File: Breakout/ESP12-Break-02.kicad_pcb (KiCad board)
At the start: 2 copper layers, 22.9 x 66.3 mm, 22 parts, among them J1 CONN_01X08, J2 CONN_01X08, J3 GS2, U1 ESP-12, U2 AP2112K-3.3TRG1

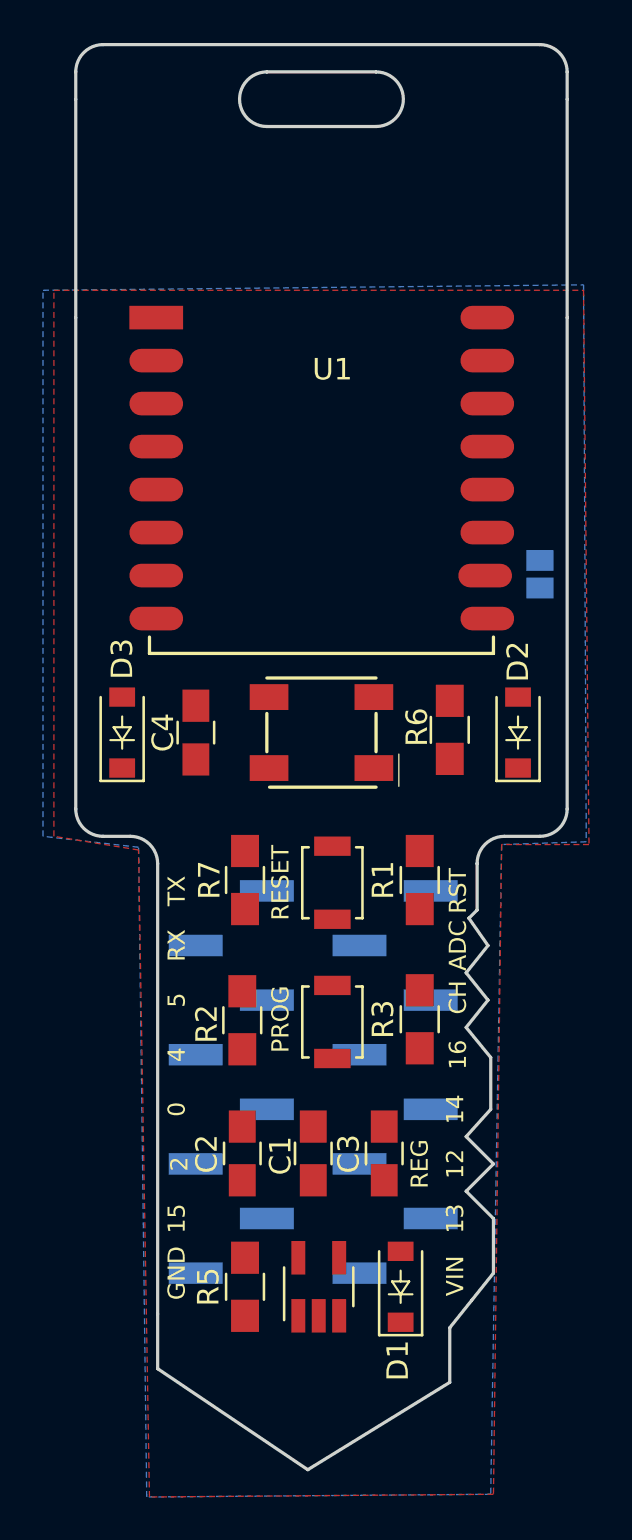
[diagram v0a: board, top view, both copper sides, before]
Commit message: Star the routing process & add OshPark logo
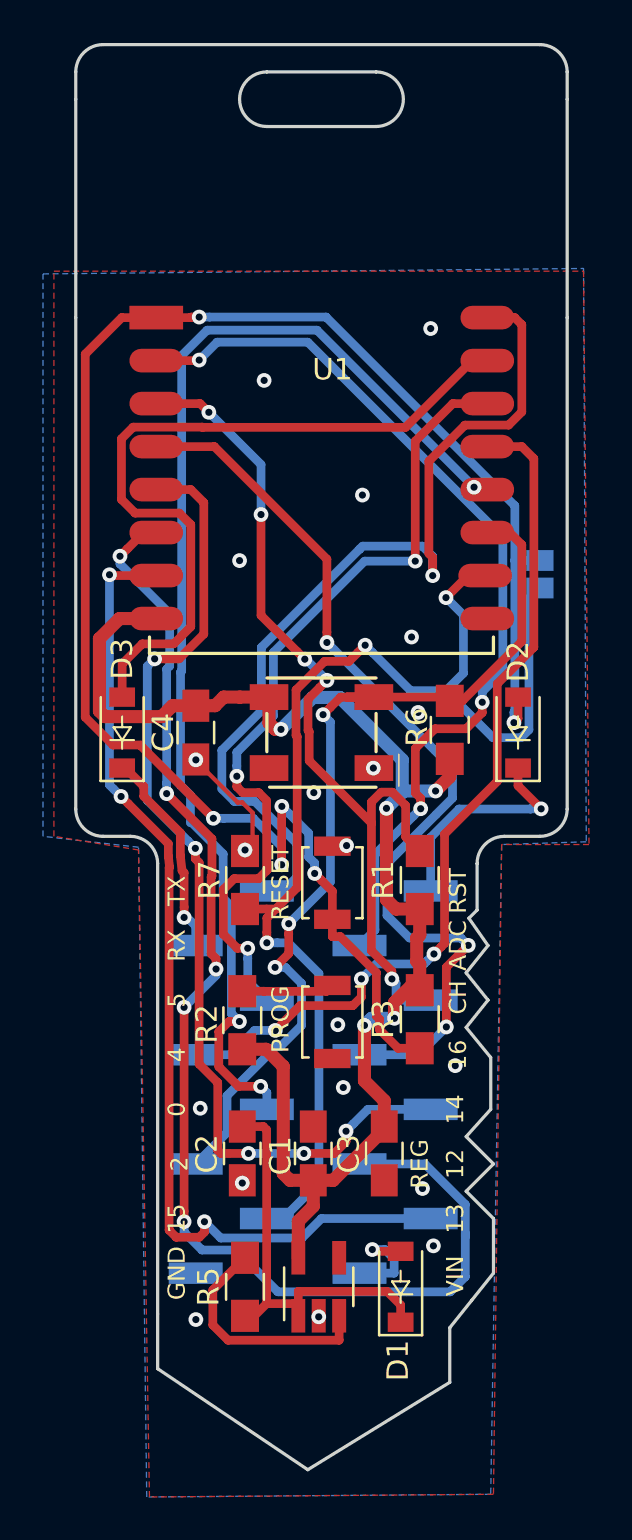
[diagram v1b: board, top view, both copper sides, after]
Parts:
- removed MazMaker***: LOGO_Silk, varios:mazmaker-600
- added G2***: LOGO2, varios:OSHpark-2-1800, B.Cu at (142.9, 51.4)
- added G3***: LOGO3, varios:OSHpark-1-2000, B.Cu at (135.9, 50.8)
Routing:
- net /RESET: track 0.00 -> 83.7 mm, vias 0 -> 6
- net /3.3V: track 0.00 -> 66.5 mm, vias 0 -> 5
- net /GPIO12: track 0.00 -> 60.7 mm, vias 0 -> 5
- net /GPIO15: track 0.00 -> 56.8 mm, vias 0 -> 3
- net /GPIO0: track 0.00 -> 55.6 mm, vias 0 -> 3
- net /GPIO13: track 0.00 -> 48.1 mm, vias 0 -> 3
- net /GPIO14: track 0.00 -> 46.1 mm, vias 0 -> 5
- net /GPIO2: track 0.00 -> 45.5 mm, vias 0 -> 3
- net /TXD: track 0.00 -> 43.3 mm, vias 0 -> 1
- net /GPIO16: track 0.00 -> 42.8 mm, vias 0 -> 3
- net /ADC: track 0.00 -> 42.3 mm, vias 0 -> 3
- net /GPIO4: track 0.00 -> 41.6 mm, vias 0 -> 3
- net /CH_PD: track 0.00 -> 40.6 mm, vias 0 -> 5
- net /GPIO5: track 0.00 -> 37.8 mm, vias 0 -> 3
- net /RXD: track 0.00 -> 34.6 mm
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
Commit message: some changes
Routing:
- net /GND: track 5.56 -> 0.04 mm, vias 20 -> 23
- net /RESET: track 83.7 -> 81.8 mm
- net /GPIO12: track 60.7 -> 61.8 mm
- net /GPIO15: track 56.8 -> 55.9 mm
- net /RXD: track 34.6 -> 35.2 mm
- net /CH_PD: track 40.6 -> 41.2 mm
